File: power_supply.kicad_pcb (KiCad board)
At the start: 2 copper layers, 101.6 x 76.2 mm, 68 parts, among them J1 USB-IN, J2 USB-A, Q1 SI4174DY, Q2 SI4463CDY, Q3 SI4463CDY, U1 LM3914, U10 FDC6392S, U11 MCP6041, U2 TPD2E001, U3 MIC2185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

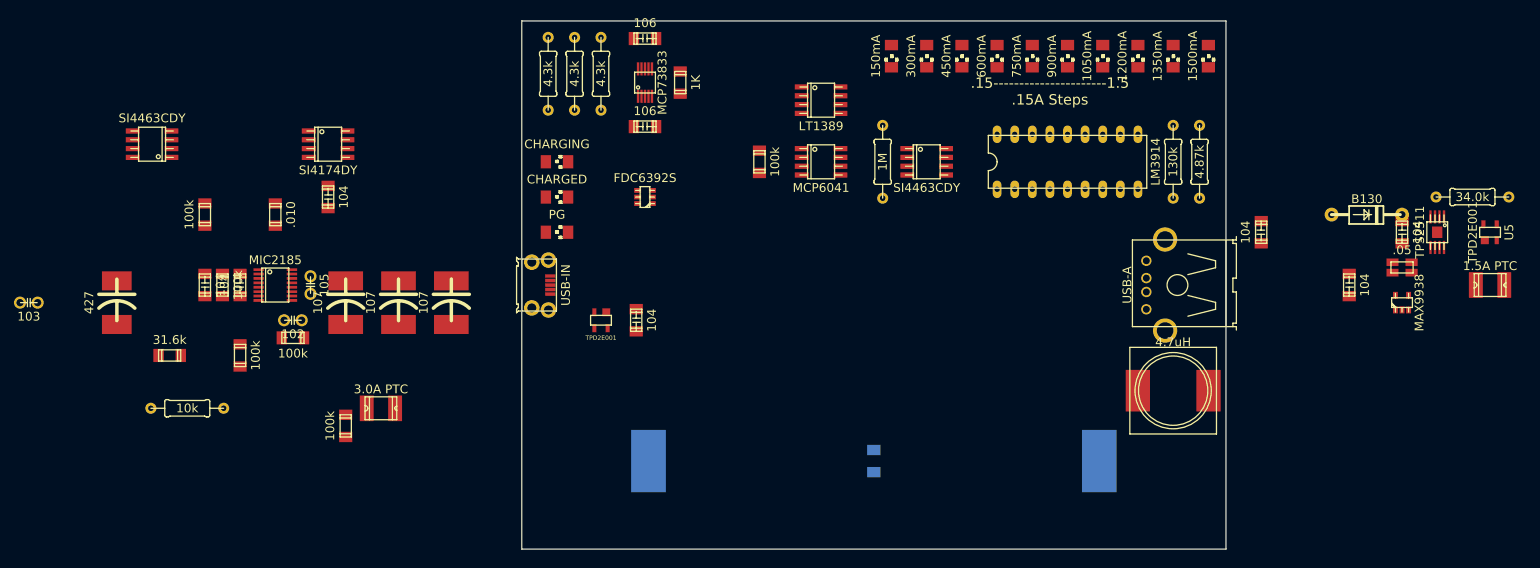
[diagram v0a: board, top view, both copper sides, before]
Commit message: Finished rev1 layout
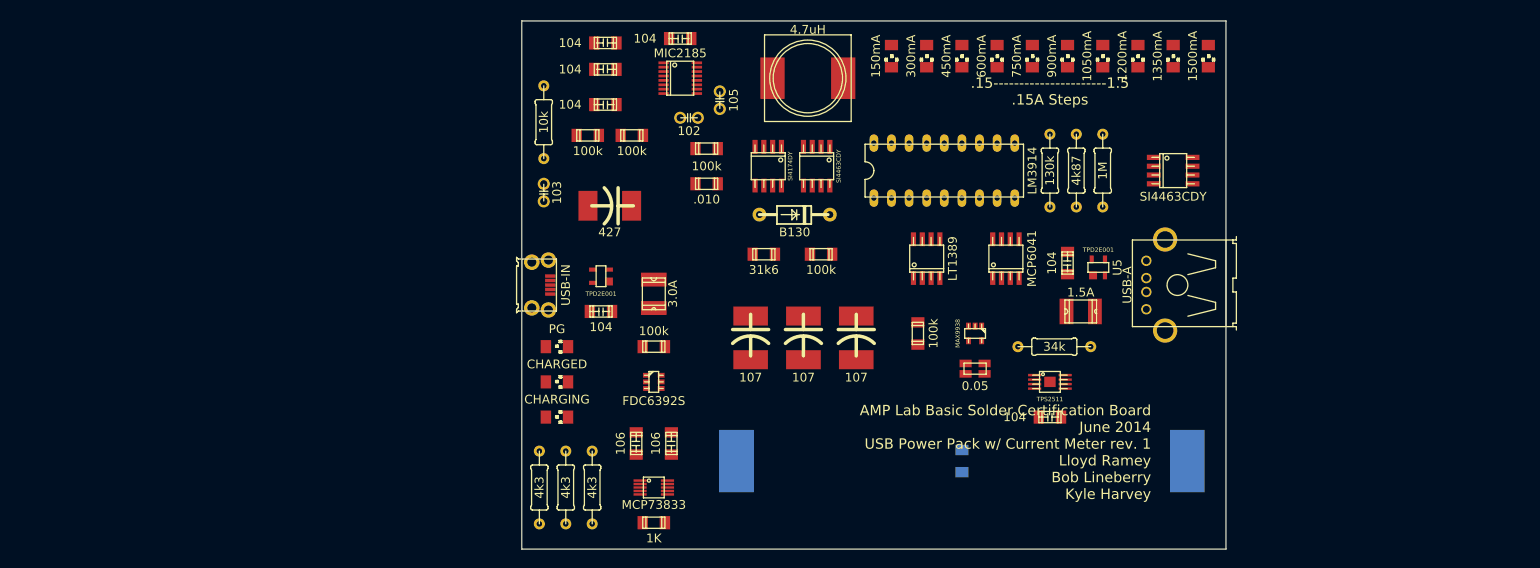
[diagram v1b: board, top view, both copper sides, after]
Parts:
- F1: value 3.0A PTC -> 3.0A
- F2: value 1.5A PTC -> 1.5A
- R1: value 4.87k -> 4k87
- R11, R6, R8: value 4.3k -> 4k3
- R14: value 31.6k -> 31k6
- R17: value .05 -> 0.05
- R7: value 34.0k -> 34k
- moved C16 102.9 mm to (175.3, 104.1), turned to 0 degrees
- moved Q2 95.9 mm to (194.9, 122.6), turned to 180 degrees
- moved R14 87.0 mm to (187.3, 135.3), turned to 0 degrees
- moved D14 82.5 mm to (191.8, 129.5)
- moved R13 77.1 mm to (195.6, 135.3)
- moved C4 76.0 mm to (155.6, 126.4), turned to 270 degrees
- moved R9 73.0 mm to (179.1, 120.0), turned to 180 degrees
- moved C1 72.5 mm to (165.1, 128.3), turned to 180 degrees
- moved L1 69.4 mm to (193.7, 109.9)
- moved R5 65.9 mm to (155.6, 116.2), turned to 270 degrees
- moved C3 65.6 mm to (164.5, 108.6), turned to 180 degrees
- moved U3 65.6 mm to (175.3, 109.9)
- moved C10 64.8 mm to (181.0, 113.0)
- moved C8 64.2 mm to (176.5, 115.6), turned to 180 degrees
- moved R7 64.1 mm to (229.2, 148.6)
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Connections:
- C9 pad 1: /VUSB -> N-0000058
- F2 pad 1: N-0000011 -> N-0000058
- J2 pad 1: N-0000011 -> N-0000058
- R17 pad I1: /VOUT -> /VREG
- R17 pad I2: /VREG -> /VOUT
- U5 pad 1: /VUSB -> N-0000058
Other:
- board text added: "AMP Lab Basic Solder Certification Board June 2014 USB Power Pack w/ Current Meter rev. 1 Lloyd Ramey Bob Lineberry Kyle Harvey"

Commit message: Began routing.
Fixed a few footprint issues.
Added through hole vias.
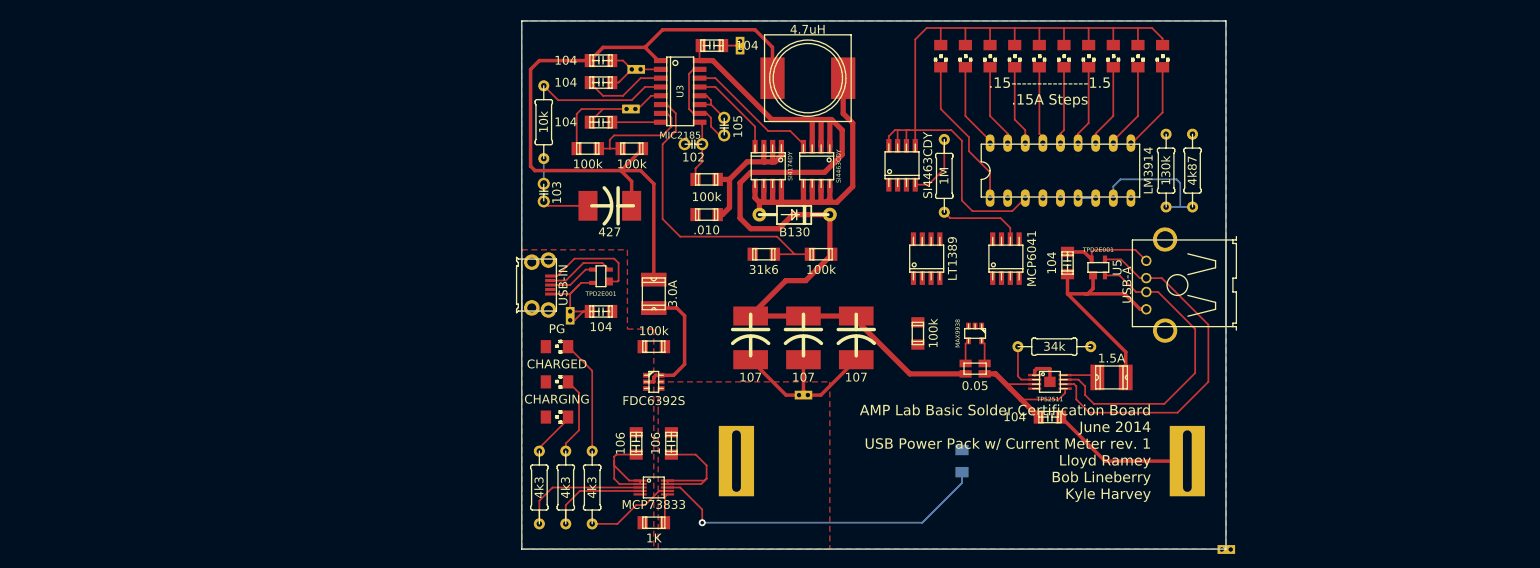
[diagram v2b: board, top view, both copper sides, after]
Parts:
- added V1: DBL_VIA, DBL_VIA, F.Cu at (168.9, 108.6)
- added V2: DBL_VIA, DBL_VIA, F.Cu at (168.1, 114.3)
- added V3: DBL_VIA, DBL_VIA, F.Cu at (183.9, 105.2)
- added V4: DBL_VIA, DBL_VIA, F.Cu at (159.4, 144.1)
- added V5: DBL_VIA, DBL_VIA, F.Cu at (193.0, 155.6)
- added V6: DBL_VIA, DBL_VIA, F.Cu at (254.1, 177.9)
- U3: footprint QSOP-16 -> so-16
- moved Q3 39.1 mm to (207.3, 122.4), turned to 0 degrees
- moved R18 22.9 mm to (213.4, 124.0)
- moved R1 16.8 mm to (249.2, 123.2)
- moved R2 16.8 mm to (245.4, 123.2)
- moved U1 16.8 mm to (230.1, 123.2)
- moved F2 10.5 mm to (237.5, 153.0)
- moved D1 7.11 mm to (212.9, 106.7)
- moved D10 6.60 mm to (244.9, 106.7)
- moved D2 5.59 mm to (216.4, 106.7)
- moved D9 5.08 mm to (241.3, 106.7)
- moved C16 4.68 mm to (179.8, 105.2), turned to 180 degrees
- moved R10 4.44 mm to (179.1, 129.5)
- moved R9 4.44 mm to (179.1, 124.5)
- moved D3 4.06 mm to (220.0, 106.7)
- moved C10 3.86 mm to (181.6, 116.8)
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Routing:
- net /VSS: track 0.00 -> 135.2 mm
- net /VREG: track 0.00 -> 134.9 mm
- net /VDISP: track 0.00 -> 112.7 mm
- net N-0000050: track 0.00 -> 102.7 mm
- net N-0000013: track 0.00 -> 53.9 mm
- net /D+: track 0.00 -> 52.4 mm
- net N-0000038: track 0.00 -> 49.6 mm, vias 0 -> 1
- net /D-: track 0.00 -> 45.4 mm
- net N-0000011: track 0.00 -> 44.9 mm
- net N-0000063: track 0.00 -> 34.0 mm
- net /VDD: track 0.00 -> 31.5 mm
- net /VOUT: track 0.00 -> 23.0 mm
- net N-0000012: track 0.00 -> 22.6 mm
- net N-000001: track 0.00 -> 21.8 mm
- net /VBAT: track 0.00 -> 19.9 mm
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- added copper zone on F.Cu, net /VBAT
- added copper zone on F.Cu, net /VDD
- added copper zone on B.Cu, net /VSS
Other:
- net class Default: clearance 0.254 -> 0.1524; via_dia 0.889 -> 1.016
- rule trace_clearance: 0.254 -> 0.1524
- board text added: ".15---------------1.5 .15A Steps"
- board text removed: ".15----------------------1.5 .15A Steps"

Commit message: More routing work
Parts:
- added V10, V9: DBL_VIA, DBL_VIA, F.Cu at (254.1, 177.9)
- added V7: DBL_VIA, DBL_VIA, F.Cu at (170.8, 174.6)
- added V8: DBL_VIA, DBL_VIA, F.Cu at (183.5, 135.3)
- moved V6 83.9 mm to (171.4, 163.2), turned to 90 degrees
- moved R16 8.89 mm to (171.4, 157.5)
- moved R12 2.01 mm to (173.4, 173.4), turned to 90 degrees
- moved U10 1.27 mm to (171.4, 152.4)
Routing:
- net /VSS: track 135.2 -> 210.9 mm
- net N-000007: track 2.54 -> 20.5 mm
- net N-0000048: track 102.7 -> 120.7 mm
- net /VSYS: track 18.8 -> 11.7 mm
- net /VDD: track 31.5 -> 36.8 mm
- net N-000009: track 4.24 -> 1.87 mm

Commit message: Finished routing
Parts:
- added R19: 100k, r_1206, F.Cu at (220.3, 142.9)
- moved V9 49.6 mm to (226.7, 136.5), turned to 90 degrees
- moved V10 39.8 mm to (229.2, 146.7)
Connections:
- U11 pad 2: /I_SENSE -> N-0000036
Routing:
- net /VREG: track 134.9 -> 212.7 mm
- net /I_SENSE: track 0.00 -> 33.4 mm
- net N-0000044: track 0.00 -> 31.3 mm
- net N-0000036: track 0.00 -> 16.2 mm
- net /VSS: track 210.9 -> 227.1 mm
- net /VBAT: track 19.9 -> 11.6 mm
- net N-000006: track 20.5 -> 23.3 mm
- added copper zone on F.Cu, net /VSS
- added copper zone on F.Cu, net /VUSB
- added copper zone on F.Cu, net N-0000057
- added copper zone on F.Cu, net N-0000060
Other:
- rule trace_min: 0.254 -> 0.1524

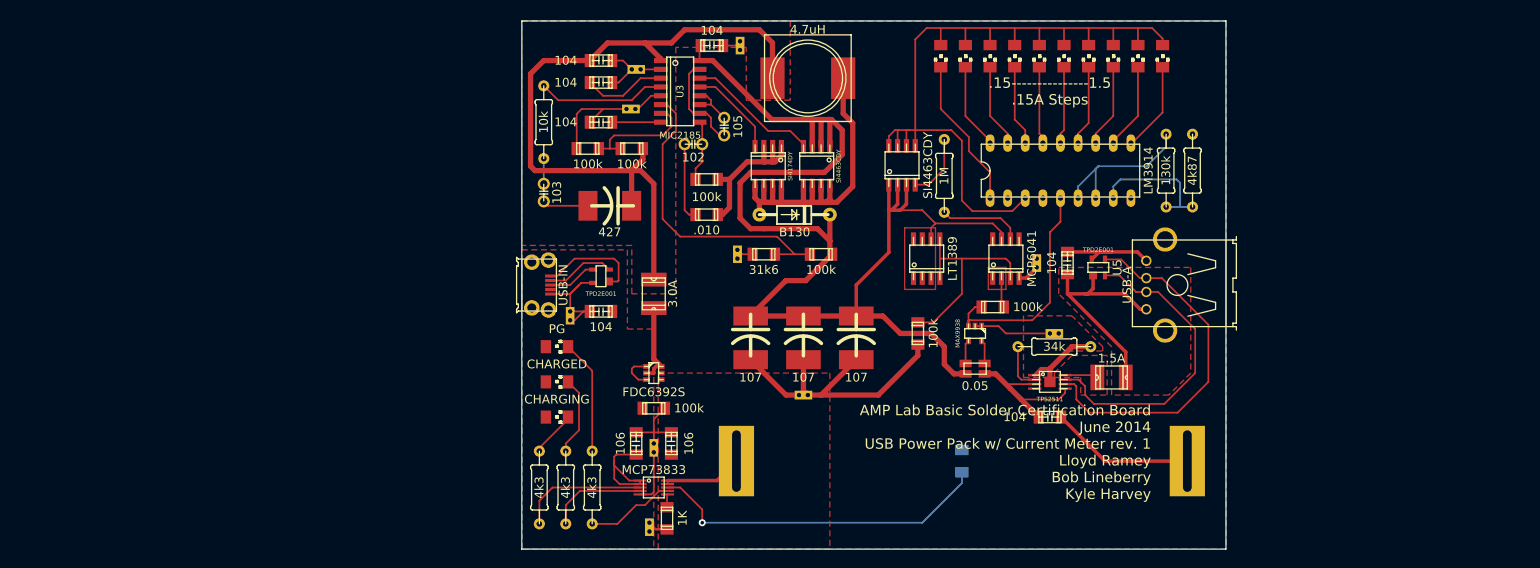
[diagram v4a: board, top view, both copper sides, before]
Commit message: Fixed issues in response to Bob's comments
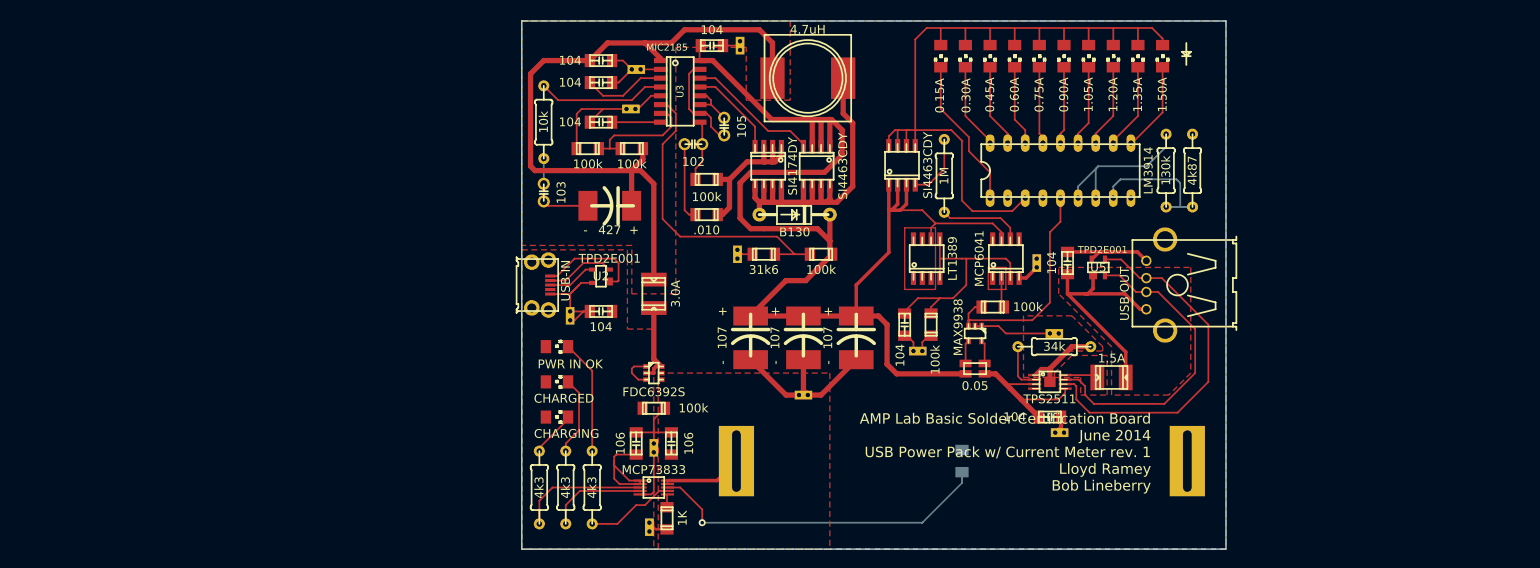
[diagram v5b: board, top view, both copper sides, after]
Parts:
- added C17: 104, c_1206, F.Cu at (207.6, 145.4)
- added V11: DBL_VIA, DBL_VIA, F.Cu at (230.0, 161.0)
- added V12: DBL_VIA, DBL_VIA, F.Cu at (209.6, 149.2)
- D1: value 150mA -> 0.15A
- D10: value 1500mA -> 1.50A
- D13: value PG -> PWR IN OK
- D2: value 300mA -> 0.30A
- D3: value 450mA -> 0.45A
- D4: value 600mA -> 0.60A
- D5: value 750mA -> 0.75A
- D6: value 900mA -> 0.90A
- D7: value 1050mA -> 1.05A
- D8: value 1200mA -> 1.20A
- D9: value 1350mA -> 1.35A
- J2: value USB-A -> USB OUT
- moved R15 2.29 mm to (211.5, 145.4)
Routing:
- net /VSS: track 227.1 -> 199.2 mm
- net N-0000043: track 31.3 -> 35.5 mm
- net /VREG: track 212.7 -> 214.6 mm
- added copper zone on F.Cu, net N-0000057
- added copper zone on F.Cu, net N-0000060
- removed copper zone on F.Cu, net N-0000062
- removed copper zone on F.Cu, net N-0000068
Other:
- board text added: "AMP Lab Basic Solder Certification Board June 2014 USB Power Pack w/ Current Meter rev. 1 Lloyd Ramey Bob Lineberry"
- board text removed: ".15---------------1.5 .15A Steps"
- board text removed: "AMP Lab Basic Solder Certification Board June 2014 USB Power Pack w/ Current Meter rev. 1 Lloyd Ramey Bob Lineberry Kyle Harvey"

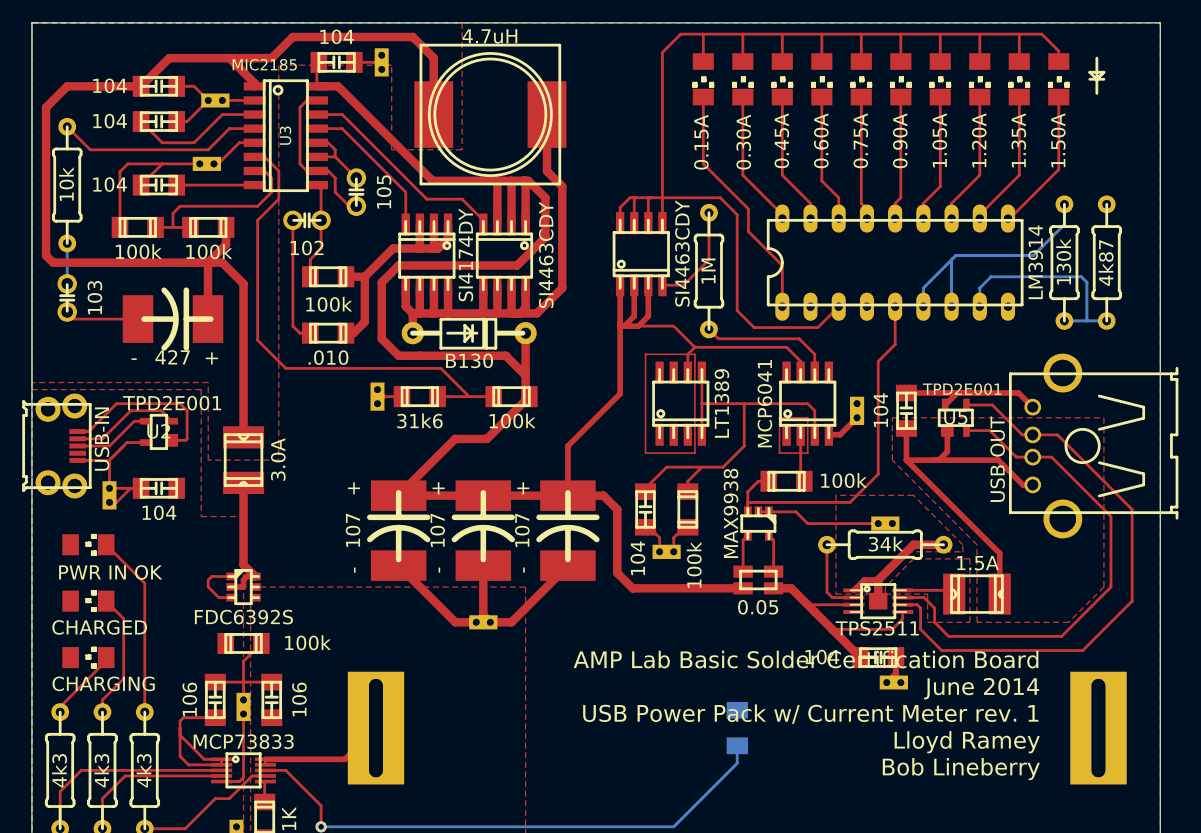
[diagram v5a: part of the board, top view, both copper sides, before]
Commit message: Added test points
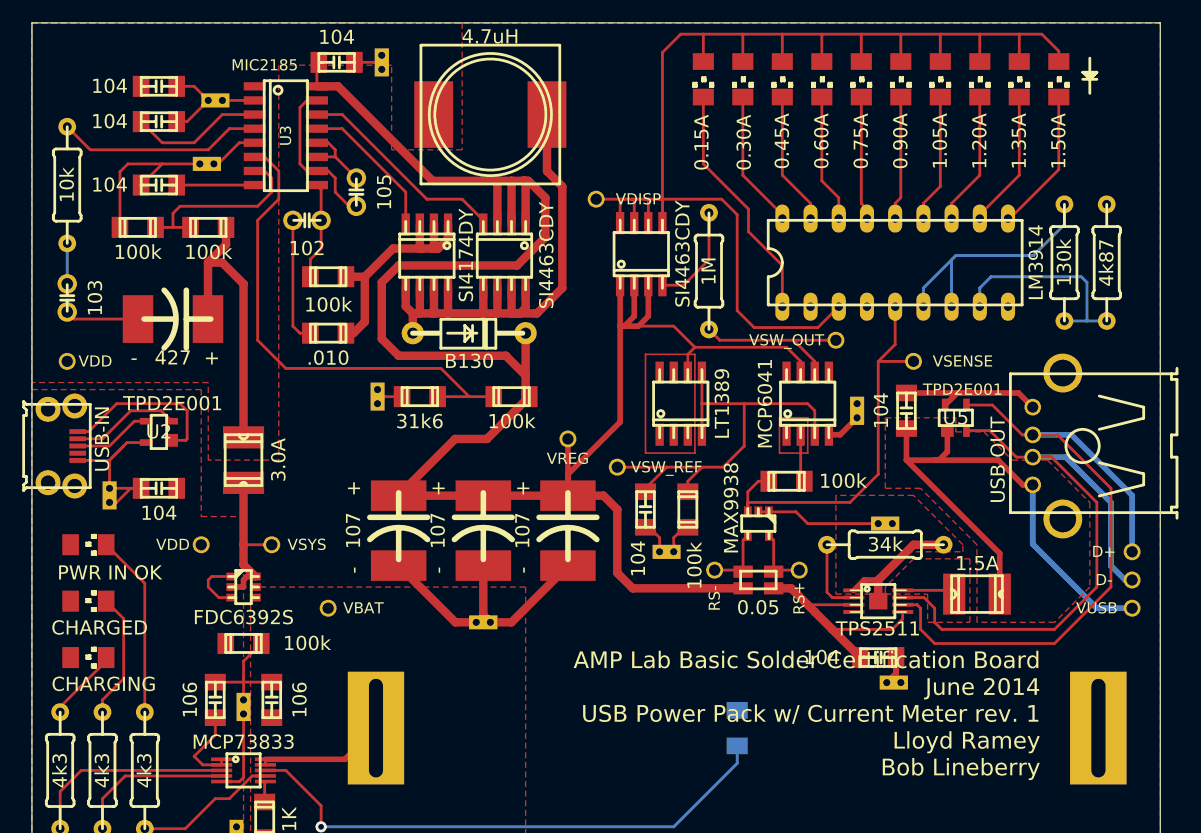
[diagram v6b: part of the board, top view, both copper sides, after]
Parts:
- added TP1: VDD, TP, F.Cu at (167.6, 148.6)
- added TP10: RS+, TP, F.Cu at (221.5, 150.9)
- added TP11: VSYS, TP, F.Cu at (174.0, 148.6)
- added TP12: VSW_OUT, TP, F.Cu at (224.8, 130.2)
- added TP13: VDISP, TP, F.Cu at (203.2, 117.5)
- added TP14: VDD, TP, F.Cu at (155.6, 132.1)
- added TP2: VUSB, TP, F.Cu at (251.5, 154.3)
- added TP3: D-, TP, F.Cu at (251.5, 151.8)
- added TP4: D+, TP, F.Cu at (251.5, 149.2)
- added TP5: VREG, TP, F.Cu at (200.7, 139.1)
- added TP6: VBAT, TP, F.Cu at (179.1, 154.3)
- added TP7: VSW_REF, TP, F.Cu at (205.1, 141.6)
- added TP8: VSENSE, TP, F.Cu at (231.8, 132.1)
- added TP9: RS-, TP, F.Cu at (213.9, 150.9)
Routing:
- net N-0000049: track 120.7 -> 26.7 mm
- net N-0000068: track 34.0 -> 50.7 mm
- net /D-: track 45.4 -> 59.9 mm
- net /D+: track 52.4 -> 64.7 mm
- net /VSS: track 199.2 -> 188.3 mm
- net /VDD: track 36.8 -> 28.1 mm
- net /VREG: track 214.6 -> 219.7 mm
- net /VDISP: track 112.7 -> 117.7 mm
- net N-0000042: track 35.5 -> 39.9 mm
- net N-0000031: track 12.1 -> 15.5 mm
- net /I_SENSE: track 33.4 -> 36.6 mm
- net N-0000032: track 3.45 -> 6.07 mm
- net /VSYS: track 11.7 -> 14.3 mm
- net N-0000035: track 3.45 -> 5.81 mm
- added copper zone on F.Cu, net N-0000049
- added copper zone on F.Cu, net N-0000068
- removed copper zone on F.Cu, net N-0000057
- removed copper zone on F.Cu, net N-0000061
